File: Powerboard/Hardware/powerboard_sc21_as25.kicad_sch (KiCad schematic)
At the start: 43 parts, among them J10 Conn_01x04_Male, J11 Conn_01x03_MountingPin, J2 Conn_01x02_Male, J3 Conn_01x02_Male, J4 Conn_01x08_Male, J9 Conn_Coaxial, Q6 MMDT2222A, Q7 RSJ250P10TL, Q8 RSJ250P10TL, U1 LTC4412xS6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

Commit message: Fixed file location and changed a trace width
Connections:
- net CAN_RX: now also U3.34 (IO5); no longer U3.27 (IO17)
- net CAN_TX: now also U3.35 (IO18); no longer U3.34 (IO5)
- net CHARGE: now also U3.36 (IO23); no longer U3.35 (IO18)
- net GND: now also U3.8 (SENSOR_VN); no longer U3.20 (IO13)
- net PDU_EN: now also U3.28 (SD2/IO9); no longer U3.25 (IO16)
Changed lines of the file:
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@@
   (junction (at 201.93 26.67) (diameter 0) (color 0 0 0 0)
   )
+  (no_connect (at 196.85 76.2))
   (no_connect (at 196.85 48.26))
   (no_connect (at 237.49 48.26))
-  (no_connect (at 196.85 50.8))
   (no_connect (at 196.85 43.18))
-  (no_connect (at 237.49 83.82))
+  (no_connect (at 196.85 73.66))
   (no_connect (at 237.49 71.12))
+  (no_connect (at 237.49 66.04))
   (no_connect (at 237.49 99.06))
   (no_connect (at 196.85 78.74))
   (no_connect (at 196.85 83.82))
-  (no_connect (at 237.49 58.42))
   (no_connect (at 237.49 63.5))
   (no_connect (at 196.85 45.72))
@@
     (stroke (width 0) (type default) (color 0 0 0 0))
   )
+  (wire (pts (xy 196.85 50.8) (xy 184.15 50.8))
+    (stroke (width 0) (type default) (color 0 0 0 0))
+  )
   (wire (pts (xy 236.22 140.97) (xy 243.84 140.97))
     (stroke (width 0) (type default) (color 0 0 0 0))
@@
     (stroke (width 0) (type default) (color 0 0 0 0))
   )
-  (wire (pts (xy 250.19 66.04) (xy 250.19 67.31))
-    (stroke (width 0) (type default) (color 0 0 0 0))
-  )
   (wire (pts (xy 162.56 33.02) (xy 157.48 33.02))
     (stroke (width 0) (type default) (color 0 0 0 0))
@@
     (stroke (width 0) (type default) (color 0 0 0 0))
   )
+  (wire (pts (xy 184.15 50.8) (xy 184.15 53.34))
+    (stroke (width 0) (type default) (color 0 0 0 0))
+  )
   (wire (pts (xy 209.55 129.54) (xy 214.63 129.54))
     (stroke (width 0) (type default) (color 0 0 0 0))
@@
     (stroke (width 0) (type default) (color 0 0 0 0))
   )
-  (wire (pts (xy 237.49 66.04) (xy 250.19 66.04))
-    (stroke (width 0) (type default) (color 0 0 0 0))
-  )
   (wire (pts (xy 201.93 26.67) (xy 201.93 29.21))
     (stroke (width 0) (type default) (color 0 0 0 0))
@@
   (label "CANH" (at 132.2324 186.436 0)
     (effects (font (size 1.27 1.27)) (justify left bottom))
-  )
-  (label "CAN_RX" (at 196.85 76.2 180)
-    (effects (font (size 1.27 1.27)) (justify right bottom))
   )
   (label "BATTSTAT1" (at 48.26 138.43 180)
     (effects (font (size 1.27 1.27)) (justify right bottom))
   )
-  (label "PDU_EN" (at 196.85 73.66 180)
-    (effects (font (size 1.27 1.27)) (justify right bottom))
-  )
-  (label "CHARGE" (at 237.49 73.66 0)
-    (effects (font (size 1.27 1.27)) (justify left bottom))
-  )
   (label "DTR" (at 69.85 173.99 0)
     (effects (font (size 1.27 1.27)) (justify left bottom))
@@
     (effects (font (size 1.27 1.27)) (justify right bottom))
   )
-  (label "CAN_TX" (at 237.49 55.88 0)
-    (effects (font (size 1.27 1.27)) (justify left bottom))
-  )
   (label "TXD" (at 69.85 170.18 0)
     (effects (font (size 1.27 1.27)) (justify left bottom))
@@
     (effects (font (size 1.27 1.27)) (justify right bottom))
   )
+  (label "CAN_TX" (at 237.49 73.66 0)
+    (effects (font (size 1.27 1.27)) (justify left bottom))
+  )
+  (label "CHARGE" (at 237.49 83.82 0)
+    (effects (font (size 1.27 1.27)) (justify left bottom))
+  )
   (label "RXD" (at 237.49 50.8 0)
+    (effects (font (size 1.27 1.27)) (justify left bottom))
+  )
+  (label "CAN_RX" (at 237.49 55.88 0)
     (effects (font (size 1.27 1.27)) (justify left bottom))
   )
@@
   (label "CAN_TX" (at 191.77 146.05 180)
     (effects (font (size 1.27 1.27)) (justify right bottom))
+  )
+  (label "PDU_EN" (at 237.49 58.42 0)
+    (effects (font (size 1.27 1.27)) (justify left bottom))
   )
   (label "LPC_24V" (at 237.49 96.52 0)
@@
     (pin "1")
   )
+  (symbol (lib_id "power:GND") (at 184.15 53.34 0) (unit 1)
+    (in_bom yes) (on_board yes) (fields_autoplaced)
+    (property "Reference" "#PWR0172" (id 0) (at 184.15 59.69 0)
+      (effects (font (size 1.27 1.27)) hide)
+    )
+    (property "Value" "GND" (id 1) (at 184.15 57.7834 0))
+    (property "Footprint" "" (id 2) (at 184.15 53.34 0)
+      (effects (font (size 1.27 1.27)) hide)
+    )
+    (property "Datasheet" "" (id 3) (at 184.15 53.34 0)
+      (effects (font (size 1.27 1.27)) hide)
+    )
+    (pin "1")
+  )
   (symbol (lib_id "power:+3.3V") (at 207.01 129.54 0) (unit 1)
     (in_bom yes) (on_board yes)
@@
     (pin "2")
   )
-  (symbol (lib_id "power:GND") (at 250.19 67.31 0) (unit 1)
-    (in_bom yes) (on_board yes) (fields_autoplaced)
-    (property "Reference" "#PWR0172" (id 0) (at 250.19 73.66 0)
-      (effects (font (size 1.27 1.27)) hide)
-    )
-    (property "Value" "GND" (id 1) (at 250.19 71.7534 0))
-    (property "Footprint" "" (id 2) (at 250.19 67.31 0)
-      (effects (font (size 1.27 1.27)) hide)
-    )
-    (property "Datasheet" "" (id 3) (at 250.19 67.31 0)
-      (effects (font (size 1.27 1.27)) hide)
-    )
-    (pin "1")
-  )
   (symbol (lib_id "power:GND") (at 243.84 163.83 0) (unit 1)
     (in_bom yes) (on_board yes)
@@
       (reference "#PWR0171") (unit 1) (value "GND") (footprint "")
     )
-    (path "/fc3282c7-c4ae-46af-bad0-e33b4abf1c37"
+    (path "/2d14feb1-4575-47c1-9b52-3c7fb892f819"
       (reference "#PWR0172") (unit 1) (value "GND") (footprint "")
     )
@@
       (reference "#PWR0178") (unit 1) (value "GND") (footprint "")
     )
+    (path "/00000000-0000-0000-0000-000061f04c1a/78a81750-ae64-476d-befb-e33924983ba6"
+      (reference "#PWR0179") (unit 1) (value "GND") (footprint "")
+    )
+    (path "/00000000-0000-0000-0000-000061f04c1a/cbb8e5e0-8be3-43f9-9538-ec5891622206"
+      (reference "#PWR0180") (unit 1) (value "GND") (footprint "")
+    )
+    (path "/00000000-0000-0000-0000-000061beb629/b0fe957c-8db3-453d-bd0e-46fcd28dcacc"
+      (reference "#PWR0181") (unit 1) (value "GND") (footprint "")
+    )
     (path "/00000000-0000-0000-0000-000061beb629/00000000-0000-0000-0000-000061c1bde2"
       (reference "C1") (unit 1) (value "0.1uF") (footprint "Capacitor_SMD:C_0603_1608Metric")
@@
       (reference "C7") (unit 1) (value "1uF") (footprint "Capacitor_SMD:C_0603_1608Metric")
     )
-    (path "/00000000-0000-0000-0000-000061beb629/fa0219bd-ef04-412e-8ab9-28366b6563fd"
-      (reference "C8") (unit 1) (value "10uF") (footprint "Capacitor_SMD:C_0805_2012Metric")
-    )
-    (path "/00000000-0000-0000-0000-000061beb629/71d361a2-0a13-42ed-95ac-084db4036962"
-      (reference "C9") (unit 1) (value "10uF") (footprint "Capacitor_SMD:C_0805_2012Metric")
+    (path "/00000000-0000-0000-0000-000061beb629/7bf2a0fa-98a7-4775-8bc6-2420389010b7"
+      (reference "C8") (unit 1) (value "10uF") (footprint "Capacitor_SMD:C_0805_2012Metric_Pad1.18x1.45mm_HandSolder")
+    )
+    (path "/00000000-0000-0000-0000-000061beb629/b216078c-1b14-49d4-8631-6753a6d6a8ec"
+      (reference "C9") (unit 1) (value "10uF") (footprint "Capacitor_SMD:C_0805_2012Metric_Pad1.18x1.45mm_HandSolder")
     )
     (path "/00000000-0000-0000-0000-000061beb629/00000000-0000-0000-0000-000061c1bf10"
@@
       (reference "C11") (unit 1) (value "0.1uF") (footprint "Capacitor_SMD:C_0603_1608Metric")
     )
-    (path "/00000000-0000-0000-0000-000061beb629/9070543a-f536-4858-b064-08c2c0881aa8"
+    (path "/00000000-0000-0000-0000-000061beb629/e164abef-1a2f-440f-acd0-cf1b93fbe6e6"
       (reference "C12") (unit 1) (value "10uF") (footprint "Capacitor_SMD:C_0805_2012Metric")
     )
-    (path "/00000000-0000-0000-0000-000061beb629/ae0251fc-94dd-4c54-92de-959d4dbadb2c"
+    (path "/00000000-0000-0000-0000-000061beb629/acbf5827-b102-4c8c-b8c3-2149de349af5"
       (reference "C13") (unit 1) (value "10uF") (footprint "Capacitor_SMD:C_0805_2012Metric")
     )
@@
       (reference "C15") (unit 1) (value "0.1uF") (footprint "Capacitor_SMD:C_0603_1608Metric")
     )
-    (path "/00000000-0000-0000-0000-000061beb629/c46192b8-c72f-41fc-8c7c-70b27a282be1"
+    (path "/00000000-0000-0000-0000-000061beb629/fbb30fac-12f5-4508-8db6-1762c0f93c00"
       (reference "C16") (unit 1) (value "2.2uF") (footprint "Capacitor_SMD:C_0805_2012Metric")
     )
@@
       (reference "C20") (unit 1) (value "47uF") (footprint "Capacitor_SMD:C_2220_5650Metric")
     )
+    (path "/00000000-0000-0000-0000-000061beb629/ae82431c-e2ed-446d-8532-24170f3914f7"
+      (reference "C21") (unit 1) (value "0.1uF") (footprint "Capacitor_SMD:C_0603_1608Metric")
+    )
     (path "/00000000-0000-0000-0000-0000620b2ec1"
       (reference "C22") (unit 1) (value "10uF") (footprint "Capacitor_SMD:C_0805_2012Metric")
@@
     )
     (path "/00000000-0000-0000-0000-000061beb629/addc896c-e29c-4cc7-8071-562dfec8452e"
-      (reference "C32") (unit 1) (value "22uF") (footprint "Capacitor_SMD:C_1206_3216Metric")
+      (reference "C32") (unit 1) (value "10uF") (footprint "Capacitor_SMD:C_0805_2012Metric")
     )
     (path "/00000000-0000-0000-0000-000061beb629/00000000-0000-0000-0000-000061c1bf6b"
@@
     )
     (path "/00000000-0000-0000-0000-000061beb629/00000000-0000-0000-0000-000061c1bdd5"
-      (reference "R9") (unit 1) (value "9.31k") (footprint "Resistor_SMD:R_0603_1608Metric")
+      (reference "R9") (unit 1) (value "2.7k") (footprint "Resistor_SMD:R_0603_1608Metric")
     )
     (path "/00000000-0000-0000-0000-000061beb629/00000000-0000-0000-0000-000061c1bdcf"
-      (reference "R10") (unit 1) (value "430k") (footprint "Resistor_SMD:R_0603_1608Metric")
+      (reference "R10") (unit 1) (value "10.5k") (footprint "Resistor_SMD:R_0603_1608Metric")
     )
     (path "/a5fc1f9e-ba65-4026-92ed-dedad5635be0"

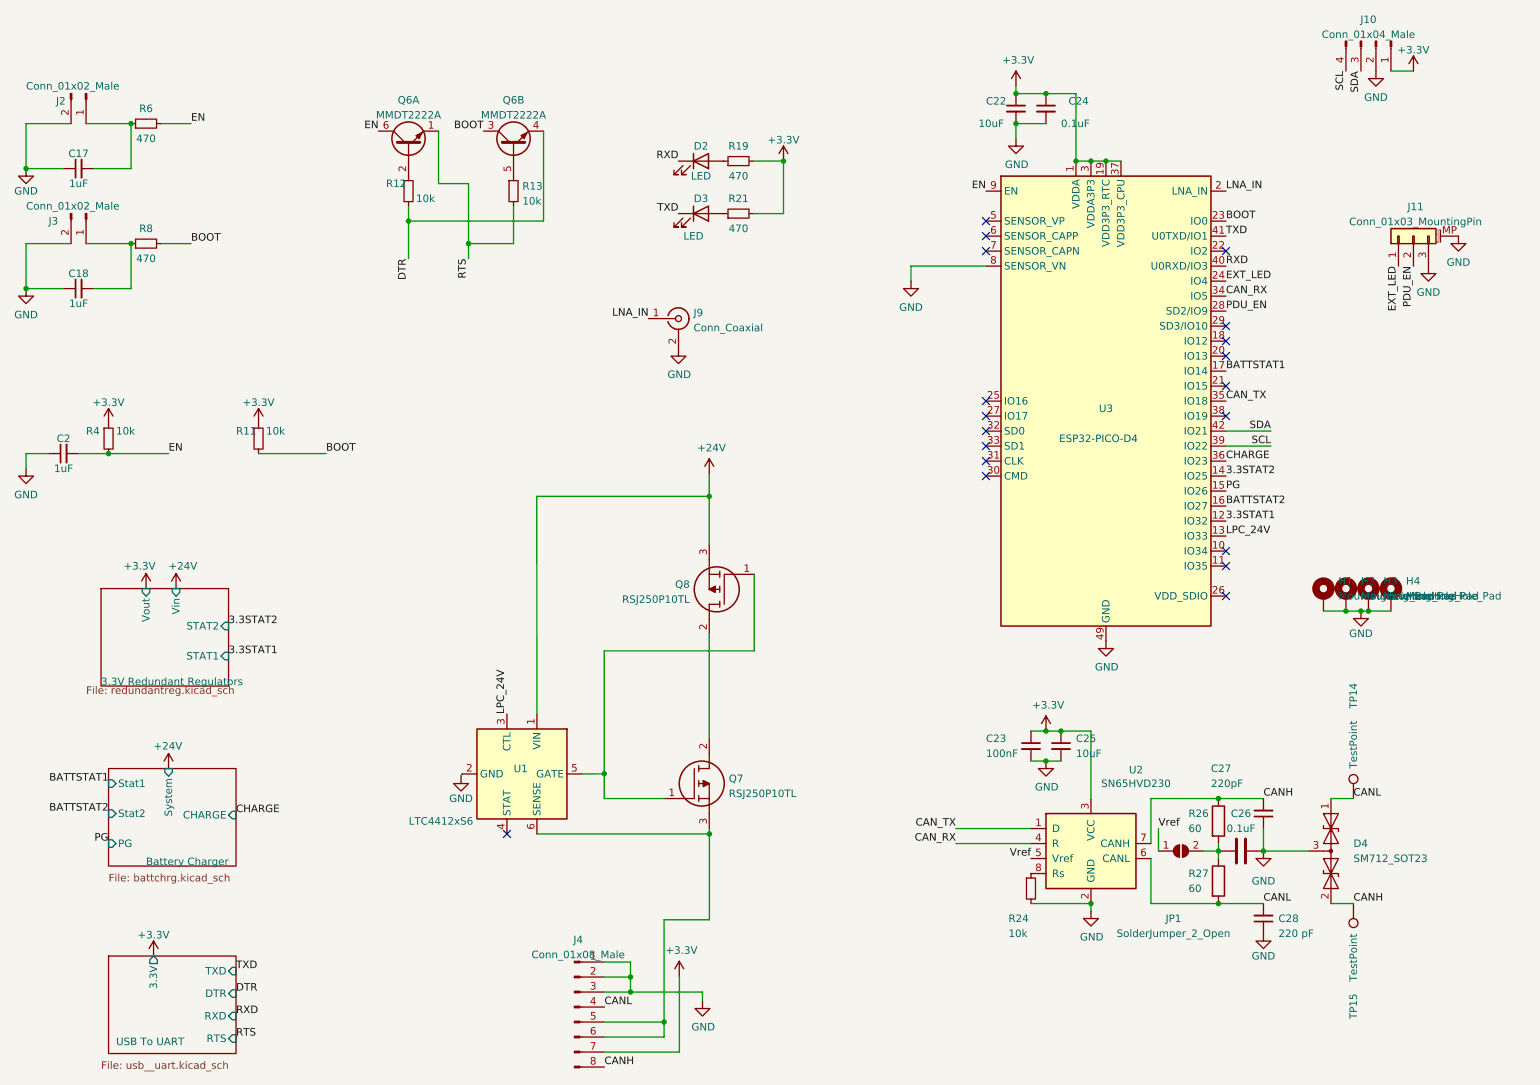
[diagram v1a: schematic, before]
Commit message: re-layed out pdu to improve buck smps stability
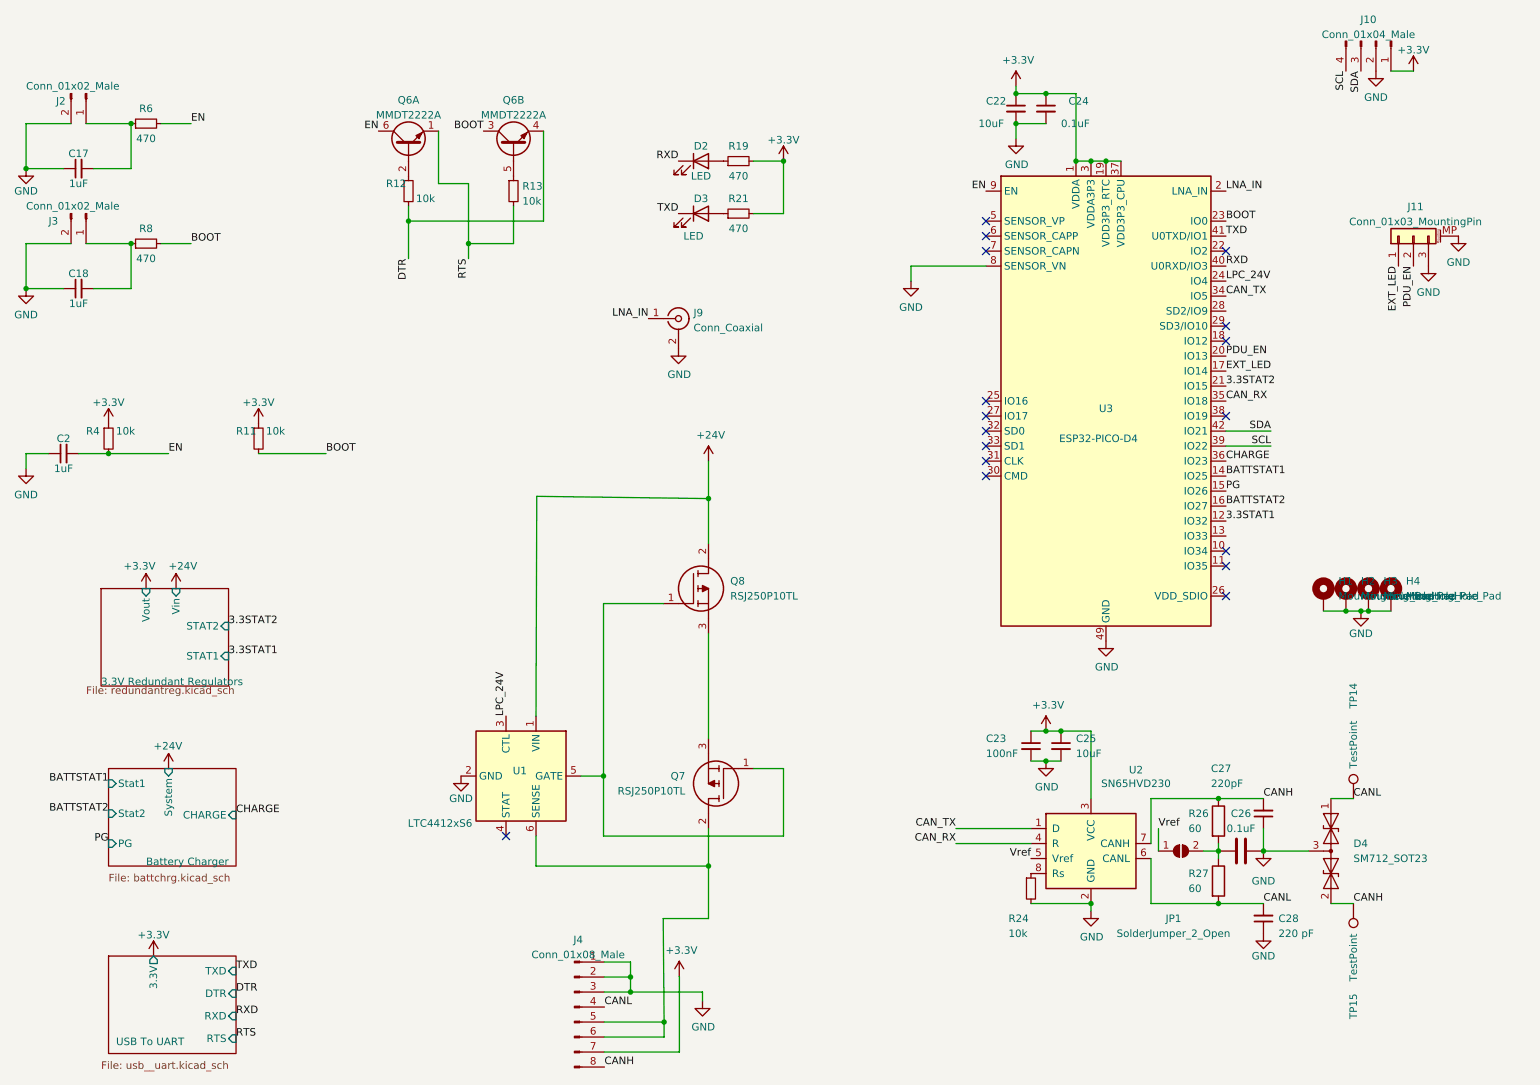
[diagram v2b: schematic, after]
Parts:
- C22: footprint Capacitor_SMD:C_0805_2012Metric -> Capacitor_SMD:C_0603_1608Metric
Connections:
- net +24V: now also Q8.2; no longer Q8.3
- net 3.3STAT2: now also U3.21 (IO15); no longer U3.14 (IO25)
- net BATTSTAT1: now also U3.14 (IO25); no longer U3.17 (IO14)
- net CAN_RX: now also U3.35 (IO18); no longer U3.34 (IO5)
- net CAN_TX: now also U3.34 (IO5); no longer U3.35 (IO18)
- net EXT_LED: now also U3.17 (IO14); no longer U3.24 (IO4)
- net LPC_24V: now also U3.24 (IO4); no longer U3.13 (IO33)
- net PDU_EN: now also U3.20 (IO13); no longer U3.28 (SD2/IO9)
- net at J4.5 (Pin_5), J4.6 (Pin_6), U1.6 (SENSE): now also Q7.2; no longer Q7.3
- new net: Q7.3, Q8.3
- no-connect marks 19 -> 17
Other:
- moved on the sheet: Q7, Q8

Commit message: Added 3v3 LED, changed LED labels on silkscreen, added Kachow
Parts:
- added D9: LED, LED_SMD:LED_0603_1608Metric, symbol Device:LED
- added R22: 470, Resistor_SMD:R_0603_1608Metric, symbol Device:R_Small
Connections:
- net +3V3: now also R22.2
- net GND: now also D9.1 (K)
- new net: D9.2 (A), R22.1
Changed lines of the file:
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@@
+    (stroke (width 0) (type default) (color 0 0 0 0))
+  )
+  (wire (pts (xy 140.97 50.8) (xy 144.78 50.8))
     (stroke (width 0) (type default) (color 0 0 0 0))
   )
@@
   )
   (wire (pts (xy 243.84 146.05) (xy 243.84 149.86))
+    (stroke (width 0) (type default) (color 0 0 0 0))
+  )
+  (wire (pts (xy 157.48 50.8) (xy 162.56 50.8))
     (stroke (width 0) (type default) (color 0 0 0 0))
   )
@@
     (pin "2")
   )
+  (symbol (lib_id "Device:LED") (at 148.59 50.8 0) (unit 1)
+    (in_bom yes) (on_board yes)
+    (property "Reference" "D9" (id 0) (at 148.59 48.26 0))
+    (property "Value" "LED" (id 1) (at 147.32 54.61 0))
+    (property "Footprint" "LED_SMD:LED_0603_1608Metric" (id 2) (at 148.59 50.8 0)
+      (effects (font (size 1.27 1.27)) hide)
+    )
+    (property "Datasheet" "~" (id 3) (at 148.59 50.8 0)
+      (effects (font (size 1.27 1.27)) hide)
+    )
+    (pin "1")
+    (pin "2")
+  )
   (symbol (lib_id "power:GND") (at 207.01 134.62 0) (unit 1)
     (in_bom yes) (on_board yes)
@@
     )
     (property "Datasheet" "" (id 3) (at 260.35 109.22 0)
+      (effects (font (size 1.27 1.27)) hide)
+    )
+    (pin "1")
+  )
+  (symbol (lib_id "power:+3.3V") (at 162.56 50.8 0) (unit 1)
+    (in_bom yes) (on_board yes) (fields_autoplaced)
+    (property "Reference" "#PWR0182" (id 0) (at 162.56 54.61 0)
+      (effects (font (size 1.27 1.27)) hide)
+    )
+    (property "Value" "+3.3V" (id 1) (at 162.56 47.2242 0))
+    (property "Footprint" "" (id 2) (at 162.56 50.8 0)
+      (effects (font (size 1.27 1.27)) hide)
+    )
+    (property "Datasheet" "" (id 3) (at 162.56 50.8 0)
       (effects (font (size 1.27 1.27)) hide)
     )
@@
     (pin "3")
   )
+  (symbol (lib_id "power:GND") (at 140.97 50.8 0) (unit 1)
+    (in_bom yes) (on_board yes)
+    (property "Reference" "#PWR0183" (id 0) (at 140.97 57.15 0)
+      (effects (font (size 1.27 1.27)) hide)
+    )
+    (property "Value" "GND" (id 1) (at 141.097 55.1942 0))
+    (property "Footprint" "" (id 2) (at 140.97 50.8 0)
+      (effects (font (size 1.27 1.27)) hide)
+    )
+    (property "Datasheet" "" (id 3) (at 140.97 50.8 0)
+      (effects (font (size 1.27 1.27)) hide)
+    )
+    (pin "1")
+  )
   (symbol (lib_id "Device:C") (at 240.03 149.86 90) (unit 1)
     (in_bom yes) (on_board yes)
@@
     )
     (pin "1")
+  )
+  (symbol (lib_id "Device:R_Small") (at 154.94 50.8 90) (unit 1)
+    (in_bom yes) (on_board yes)
+    (property "Reference" "R22" (id 0) (at 154.94 48.26 90))
+    (property "Value" "470" (id 1) (at 154.94 53.34 90))
+    (property "Footprint" "Resistor_SMD:R_0603_1608Metric" (id 2) (at 154.94 50.8 0)
+      (effects (font (size 1.27 1.27)) hide)
+    )
+    (property "Datasheet" "~" (id 3) (at 154.94 50.8 0)
+      (effects (font (size 1.27 1.27)) hide)
+    )
+    (pin "1")
+    (pin "2")
   )
   (symbol (lib_id "iclr:RSJ250P10TL") (at 142.24 107.95 0) (unit 1)
@@
       (reference "#PWR0181") (unit 1) (value "GND") (footprint "")
     )
+    (path "/152c86a3-a086-4449-a519-a28808e87993"
+      (reference "#PWR0182") (unit 1) (value "+3.3V") (footprint "")
+    )
+    (path "/58d7d269-9410-4f6d-b863-3ba5a44dcf27"
+      (reference "#PWR0183") (unit 1) (value "GND") (footprint "")
+    )
     (path "/00000000-0000-0000-0000-000061beb629/00000000-0000-0000-0000-000061c1bde2"
       (reference "C1") (unit 1) (value "0.1uF") (footprint "Capacitor_SMD:C_0603_1608Metric")
@@
       (reference "D8") (unit 1) (value "SP0503BAHT") (footprint "Package_TO_SOT_SMD:SOT-143")
     )
+    (path "/048489de-6a43-4ccf-9629-8fdb92287533"
+      (reference "D9") (unit 1) (value "LED") (footprint "LED_SMD:LED_0603_1608Metric")
+    )
     (path "/4485c930-129d-46dc-91ce-94bf0e81babd"
       (reference "H1") (unit 1) (value "MountingHole_Pad") (footprint "MountingHole:MountingHole_3.2mm_M3_DIN965_Pad")
@@
       (reference "R21") (unit 1) (value "470") (footprint "Resistor_SMD:R_0603_1608Metric")
     )
+    (path "/90f614bf-dfa6-4df0-aac7-eac9b30b7332"
+      (reference "R22") (unit 1) (value "470") (footprint "Resistor_SMD:R_0603_1608Metric")
+    )
     (path "/367b9243-e298-4361-927a-ff1499c679d9"
